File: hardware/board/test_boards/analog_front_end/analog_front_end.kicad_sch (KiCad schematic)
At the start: 14 parts, among them J1 Conn_01x20_Female, J2 Conn_01x20_Female, U6 LM27762

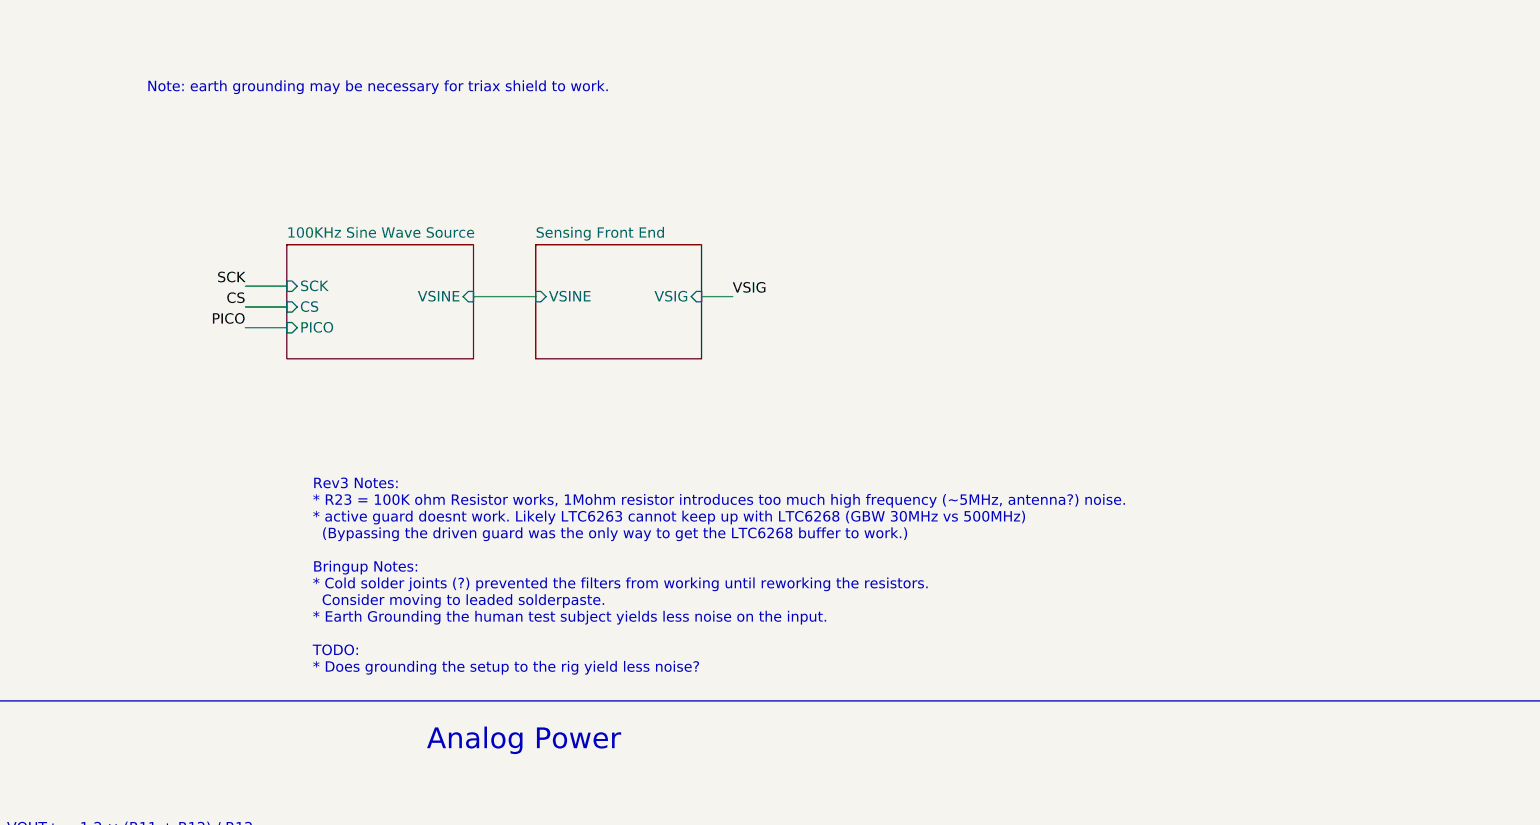
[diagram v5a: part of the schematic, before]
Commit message: implement slow/fast iir windows
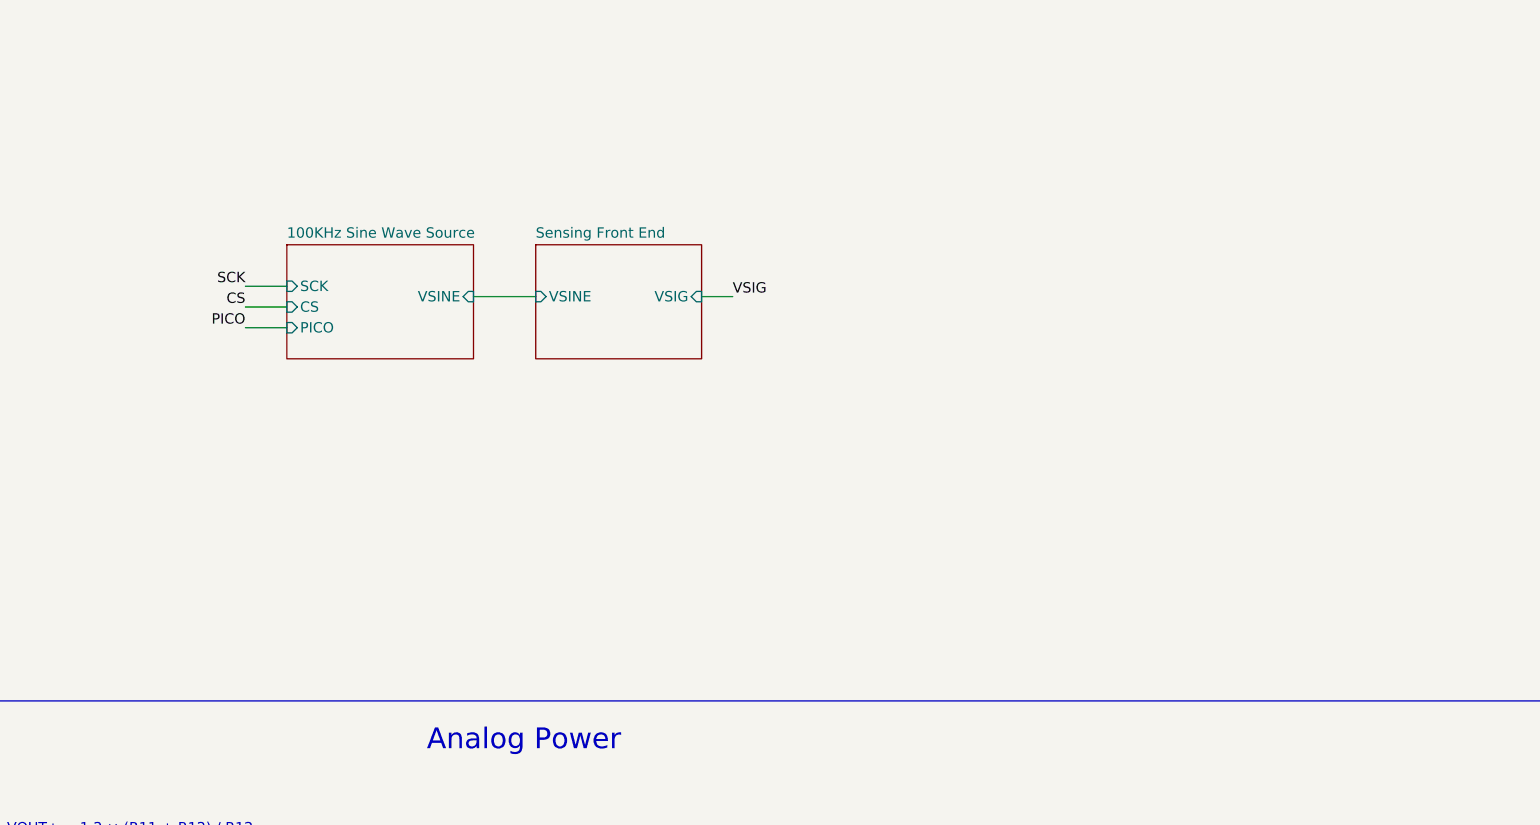
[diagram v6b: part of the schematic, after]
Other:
- note removed: "Note: earth grounding may be necessary for triax shield to work."
- note removed: "Rev3 Notes: * R23 = 100K ohm Resistor works, 1Mohm resistor introduces too much high frequency (~5MHz, antenna?) noise. * active guard doesnt work. Likely LTC6263 cannot keep up with LTC6268 (GBW 30MHz vs 500MHz) (Bypassing the driven guard was the only way to get the LTC6268 buffer to work.) Bringup Notes: * Cold solder joints (?) prevented the filters from working until reworking the resistors.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"
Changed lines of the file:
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@@
-    (effects (font (size 1.27 1.27)) (justify left bottom))
-  )
-  (text "Rev3 Notes:\n* R23 = 100K ohm Resistor works, 1Mohm resistor introduces too much high frequency (~5MHz, antenna?) noise.\n* active guard doesnt work. Likely LTC6263 cannot keep up with LTC6268 (GBW 30MHz vs 500MHz)\n  (Bypassing the driven guard was the only way to get the LTC6268 buffer to work.)\n\nBringup Notes:\n* Cold solder joints (?) prevented the filters from working until reworking the resistors.\n  Consider moving to leaded solderpaste.\n* Earth Grounding the human test subject yields less noise on the input.\n\nTODO: \n* Does grounding the setup to the rig yield less noise?"
-    (at 122.555 102.235 0)
     (effects (font (size 1.27 1.27)) (justify left bottom))
   )
@@
     (effects (font (size 1.27 1.27)) (justify left bottom))
   )
-  (text "Note: earth grounding may be necessary for triax shield to work."
-    (at 102.235 31.115 0)
-    (effects (font (size 1.27 1.27)) (justify left bottom))
-  )

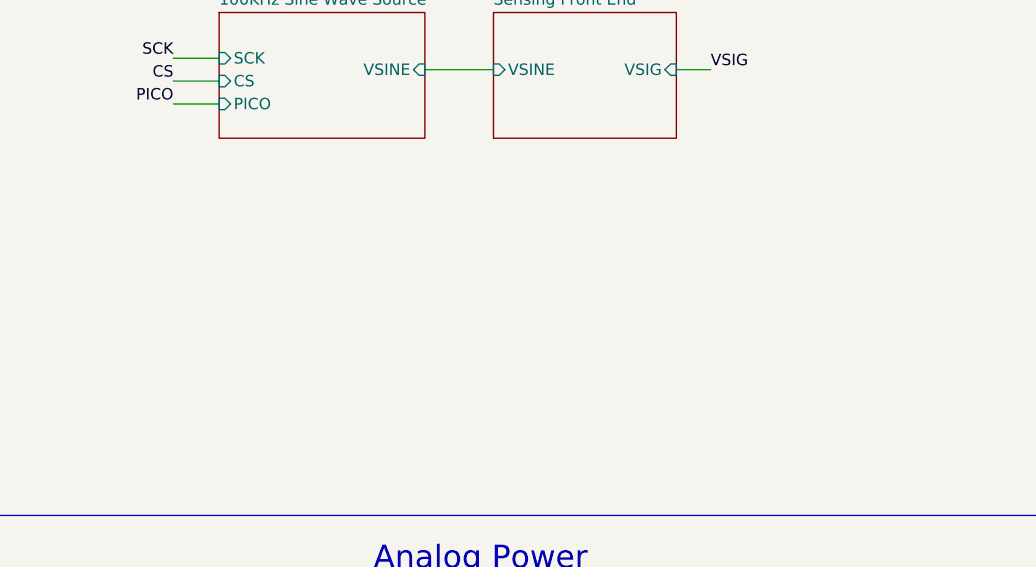
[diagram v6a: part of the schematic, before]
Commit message: draft ads7029 pio driver
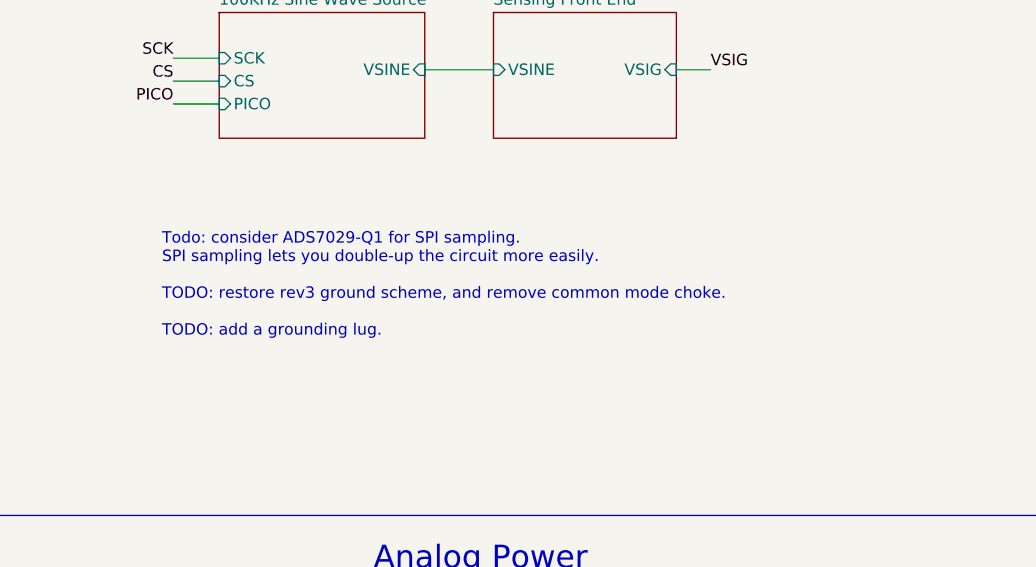
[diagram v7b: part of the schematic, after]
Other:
- note added: "Todo: consider ADS7029-Q1 for SPI sampling. SPI sampling lets you double-up the circuit more easily. TODO: restore rev3 ground scheme, and remove common mode choke. TODO: add a grounding lug."
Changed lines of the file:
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@@
+    (effects (font (size 1.27 1.27)) (justify left bottom))
+  )
+  (text "Todo: consider ADS7029-Q1 for SPI sampling.\nSPI sampling lets you double-up the circuit more easily.\n\nTODO: restore rev3 ground scheme, and remove common mode choke.\n\nTODO: add a grounding lug."
+    (at 113.03 85.725 0)
     (effects (font (size 1.27 1.27)) (justify left bottom))
   )
